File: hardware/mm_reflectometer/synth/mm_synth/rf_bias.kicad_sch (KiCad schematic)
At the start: 59 parts

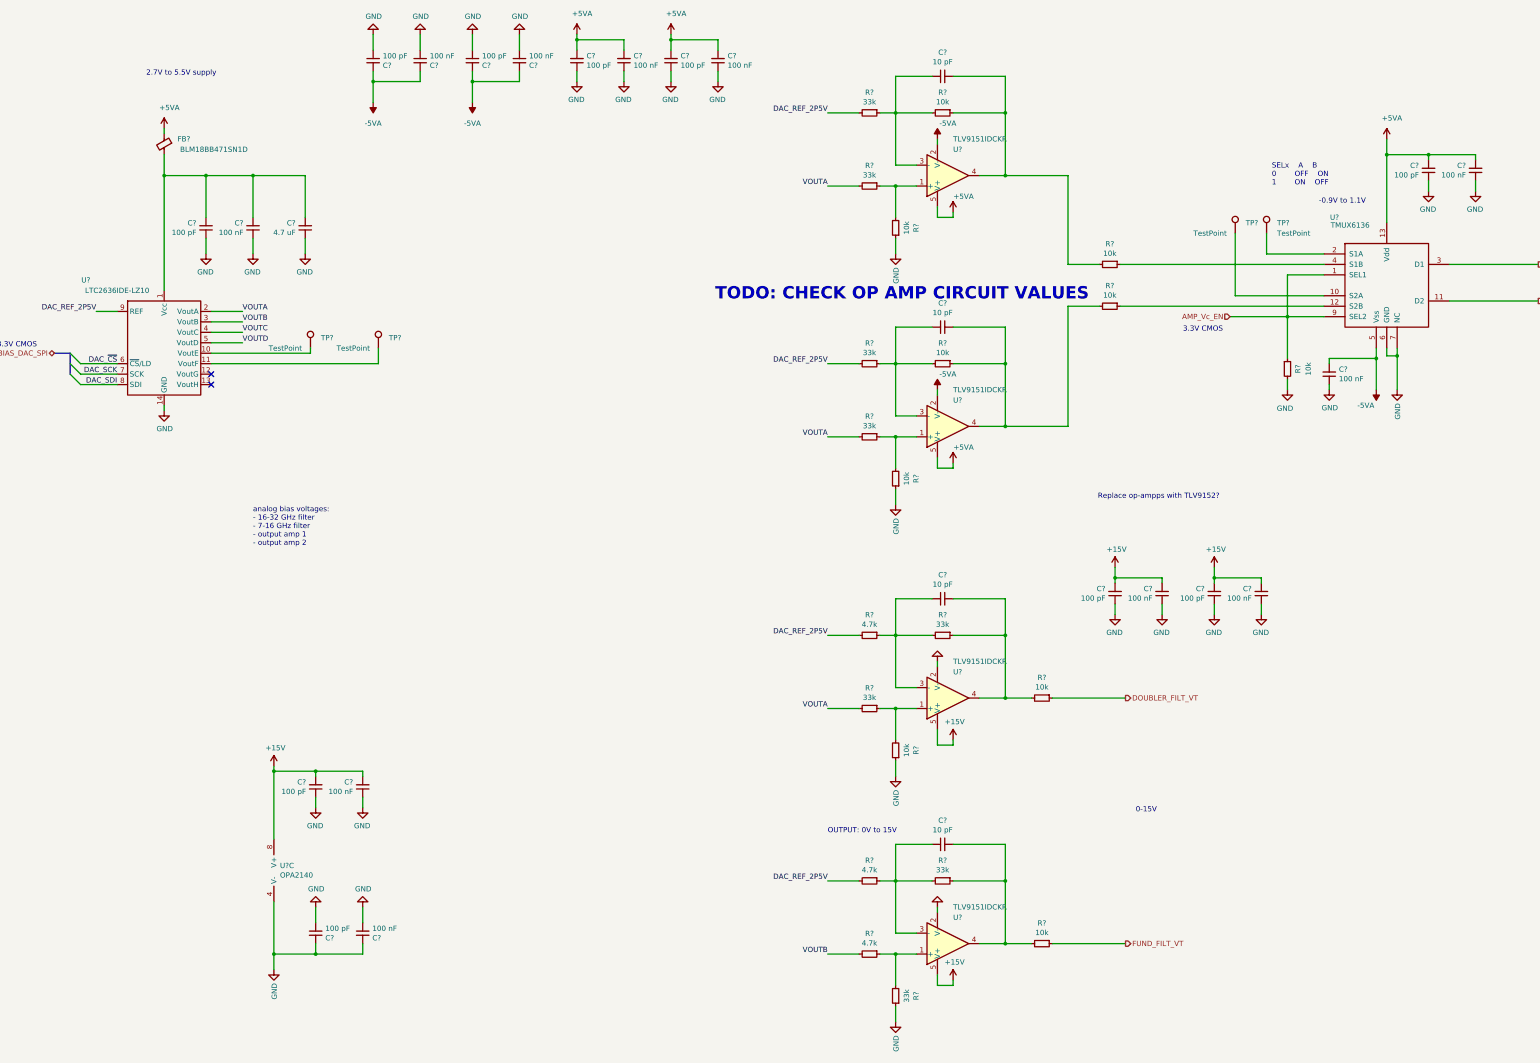
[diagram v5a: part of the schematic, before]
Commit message: work on mm synth schematic - control signals and footprint assignments
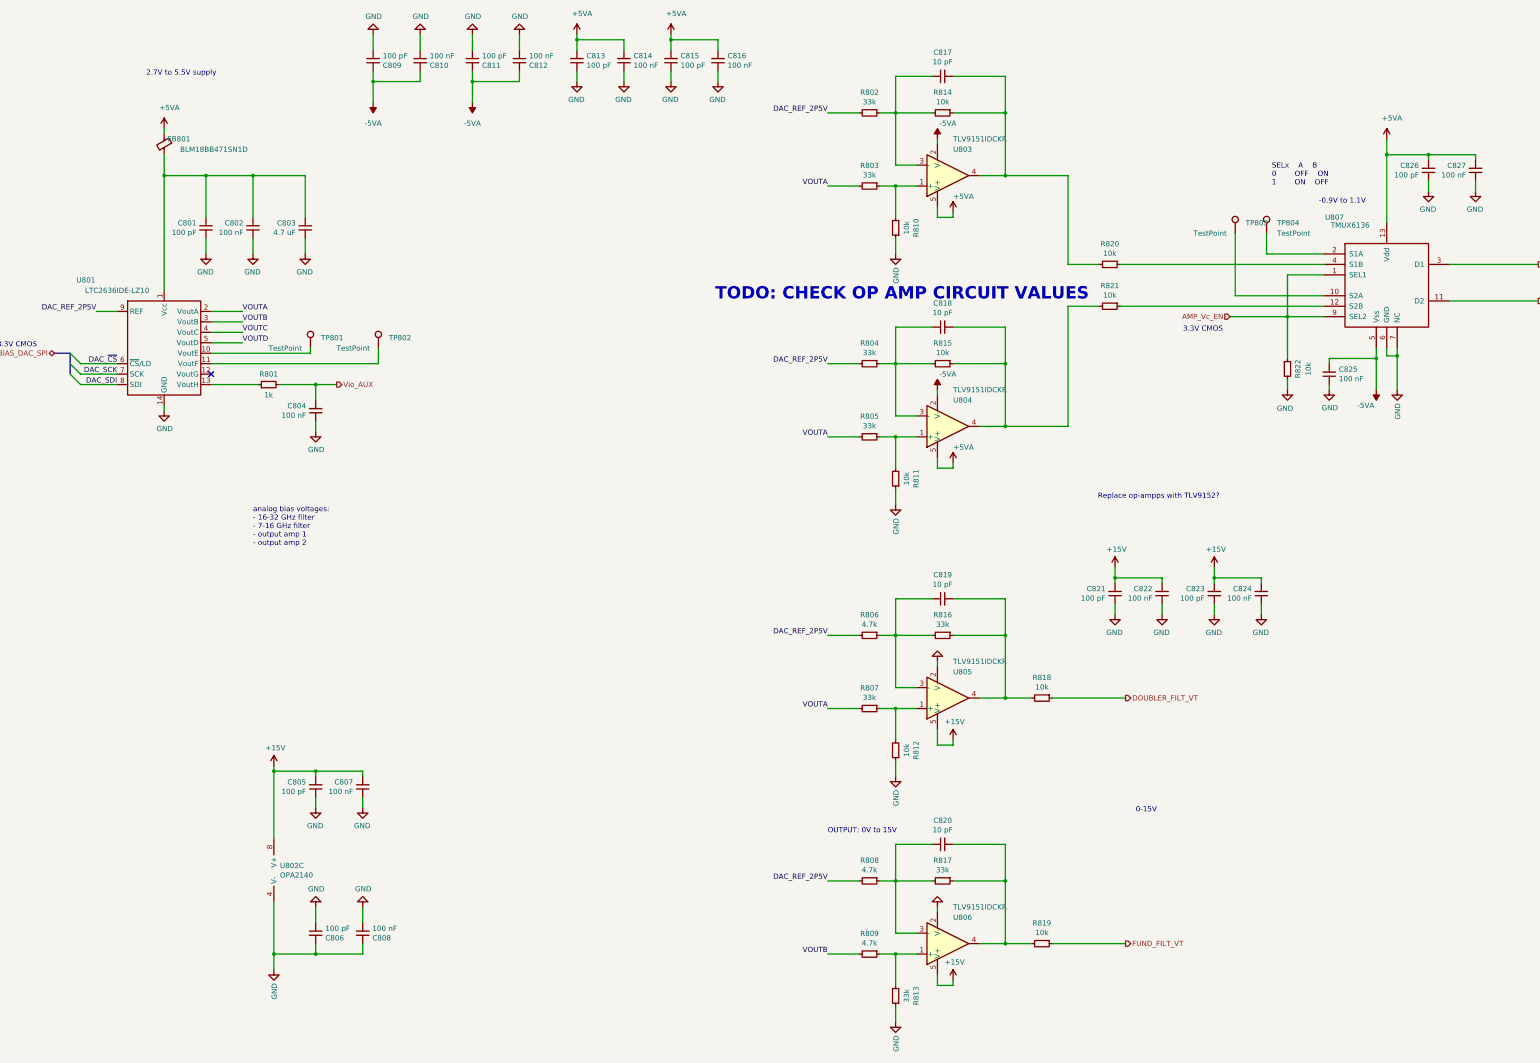
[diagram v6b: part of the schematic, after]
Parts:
- added C804: 100 nF, Capacitor_SMD:C_0402_1005Metric, symbol Device:C_Small
- added R801: 1k, Resistor_SMD:R_0402_1005Metric, symbol Device:R_Small
- TP801, TP802, TP803, TP804: renamed from TP?; footprint (none) -> TestPoint:TestPoint_Pad_D1.5mm
- gave numbers to parts that had none: 55
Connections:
- net GND: now also C804.1
- net at U801.13 (VoutH): now also R801.1
- net DAC_~CS renamed DAC_~{CS}
- new net Vio_AUX: C804.2, R801.2
- no-connect marks 2 -> 1

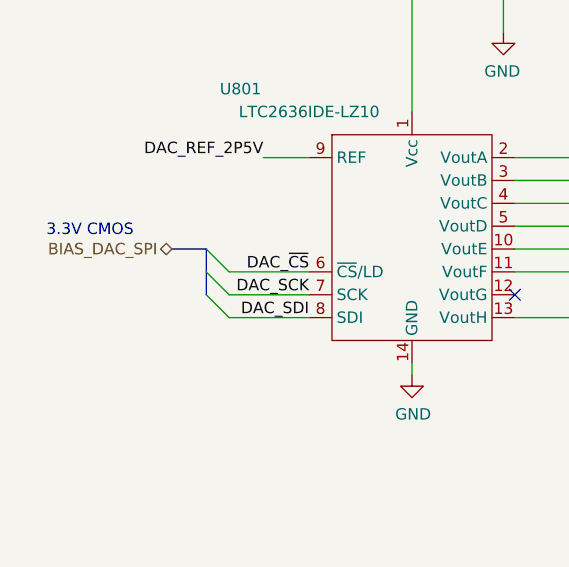
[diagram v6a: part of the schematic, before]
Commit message: added aux high speed io connector, fixed hierarchical buses
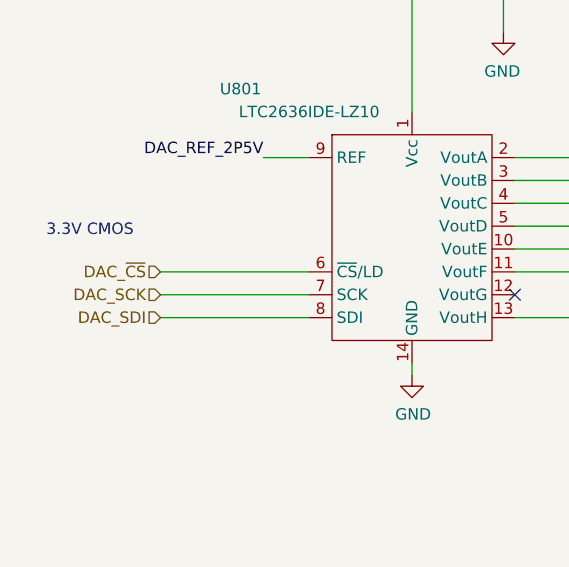
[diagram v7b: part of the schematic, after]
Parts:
- FB801: footprint (none) -> Inductor_SMD:L_0603_1608Metric
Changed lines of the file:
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@@
   (junction (at 361.95 52.07) (diameter 0.9144) (color 0 0 0 0))
   (no_connect (at 66.04 105.41))
-  (bus_entry (at 31.75 100.33) (size 2.54 2.54)
-    (stroke (width 0.1524) (type solid) (color 0 0 0 0))
-  )
-  (bus_entry (at 31.75 102.87) (size 2.54 2.54)
-    (stroke (width 0.1524) (type solid) (color 0 0 0 0))
-  )
-  (bus_entry (at 31.75 105.41) (size 2.54 2.54)
-    (stroke (width 0.1524) (type solid) (color 0 0 0 0))
-  )
-  (wire (pts (xy 34.29 102.87) (xy 43.18 102.87))
-    (stroke (width 0) (type solid) (color 0 0 0 0))
-  )
-  (wire (pts (xy 34.29 105.41) (xy 43.18 105.41))
-    (stroke (width 0) (type solid) (color 0 0 0 0))
-  )
-  (wire (pts (xy 34.29 107.95) (xy 43.18 107.95))
+  (wire (pts (xy 26.67 102.87) (xy 43.18 102.87))
+    (stroke (width 0) (type solid) (color 0 0 0 0))
+  )
+  (wire (pts (xy 26.67 105.41) (xy 43.18 105.41))
+    (stroke (width 0) (type solid) (color 0 0 0 0))
+  )
+  (wire (pts (xy 26.67 107.95) (xy 43.18 107.95))
     (stroke (width 0) (type solid) (color 0 0 0 0))
   )
@@
   )
   (wire (pts (xy 373.38 58.42) (xy 373.38 60.96))
-    (stroke (width 0) (type solid) (color 0 0 0 0))
-  )
-  (bus (pts (xy 27.94 100.33) (xy 31.75 100.33))
-    (stroke (width 0) (type solid) (color 0 0 0 0))
-  )
-  (bus (pts (xy 31.75 100.33) (xy 31.75 105.41))
     (stroke (width 0) (type solid) (color 0 0 0 0))
   )
@@
     (effects (font (size 1.27 1.27)) (justify right bottom))
   )
-  (label "DAC_~{CS}" (at 43.18 102.87 180)
-    (effects (font (size 1.27 1.27)) (justify right bottom))
-  )
-  (label "DAC_SCK" (at 43.18 105.41 180)
-    (effects (font (size 1.27 1.27)) (justify right bottom))
-  )
-  (label "DAC_SDI" (at 43.18 107.95 180)
-    (effects (font (size 1.27 1.27)) (justify right bottom))
-  )
   (label "VOUTA" (at 73.66 90.17 0)
     (effects (font (size 1.27 1.27)) (justify left bottom))
@@
     (effects (font (size 1.27 1.27)) (justify right bottom))
   )
-  (hierarchical_label "BIAS_DAC_SPI" (shape bidirectional) (at 27.94 100.33 180)
+  (hierarchical_label "DAC_~{CS}" (shape input) (at 26.67 102.87 180)
+    (effects (font (size 1.27 1.27)) (justify right))
+  )
+  (hierarchical_label "DAC_SCK" (shape input) (at 26.67 105.41 180)
+    (effects (font (size 1.27 1.27)) (justify right))
+  )
+  (hierarchical_label "DAC_SDI" (shape input) (at 26.67 107.95 180)
     (effects (font (size 1.27 1.27)) (justify right))
   )
@@
       (effects (font (size 1.27 1.27)) (justify left))
     )
-    (property "Footprint" "" (id 2) (at 56.388 49.53 90)
-      (effects (font (size 1.27 1.27)) hide)
-    )
+    (property "Footprint" "Inductor_SMD:L_0603_1608Metric" (id 2) (at 56.388 49.53 90)
+      (effects (font (size 1.27 1.27)) hide)
+    )

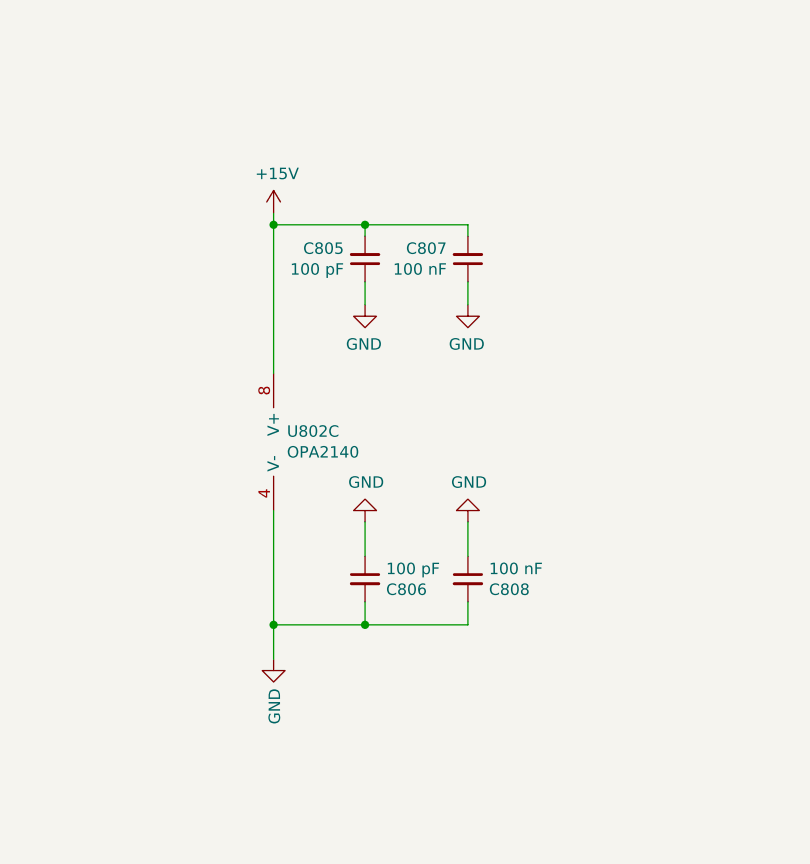
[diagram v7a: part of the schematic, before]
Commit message: schematic cleanup, erc
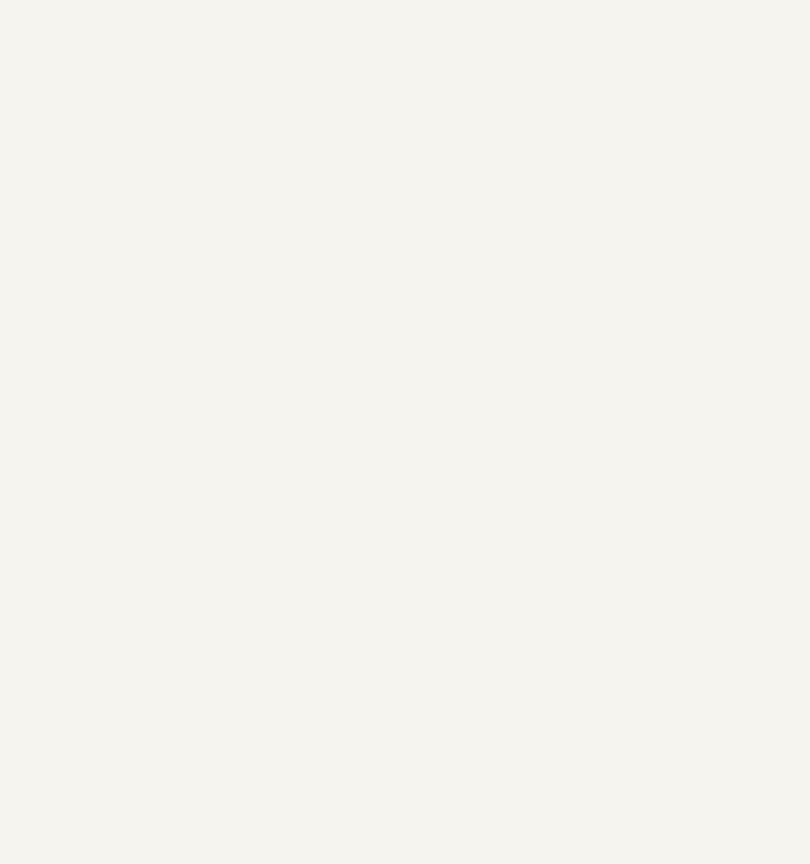
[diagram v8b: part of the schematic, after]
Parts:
- removed C805, C806: 100 pF, Capacitor_SMD:C_0402_1005Metric, symbol Device:C_Small
- removed C807, C808: 100 nF, Capacitor_SMD:C_0402_1005Metric, symbol Device:C_Small
- removed U802: OPA2140, Package_SO:MSOP-8_3x3mm_P0.65mm, symbol vna_mm_synth-rescue:Opamp_Dual_Generic-Device
- U807: footprint Package_SO:TSSOP-14_4.4x5mm_P0.65mm -> Package_SO:TSSOP-16_4.4x5mm_P0.65mm
